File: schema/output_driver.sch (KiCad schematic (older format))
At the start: 9 parts, among them Q3 BC107B, U11 HEF4013, U4 HEF4538

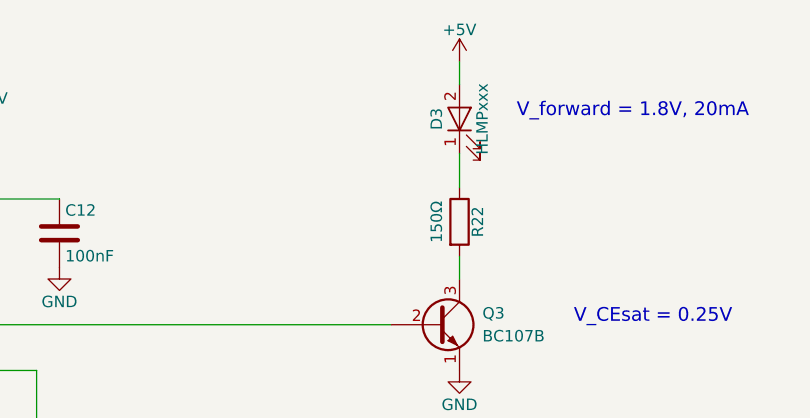
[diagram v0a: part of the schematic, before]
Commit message: Add missing decoupling capacitors
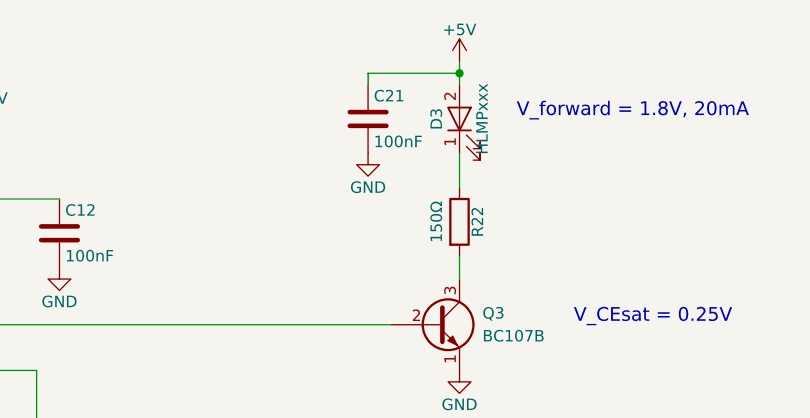
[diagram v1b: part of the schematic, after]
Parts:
- added C21: 100nF, symbol C
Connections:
- wire segments 28 -> 30
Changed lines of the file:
@@
 $EndComp
 $Comp
-L +5V #PWR32
+L +5V #PWR35
 U 1 1 5910A522
 P 8550 2350
-F 0 "#PWR32" H 8550 2200 50  0001 C CNN
+F 0 "#PWR35" H 8550 2200 50  0001 C CNN
 F 1 "+5V" H 8550 2490 50  0000 C CNN
 F 2 "" H 8550 2350 50  0000 C CNN
@@
 $EndComp
 $Comp
-L GND #PWR33
+L GND #PWR36
 U 1 1 5910A53C
 P 8550 3700
-F 0 "#PWR33" H 8550 3450 50  0001 C CNN
+F 0 "#PWR36" H 8550 3450 50  0001 C CNN
 F 1 "GND" H 8550 3550 50  0000 C CNN
 F 2 "" H 8550 3700 50  0000 C CNN
@@
 	2600 2800 2600 2600
 $Comp
-L +5V #PWR22
+L +5V #PWR24
 U 1 1 592FDE80
 P 2600 2700
-F 0 "#PWR22" H 2600 2550 50  0001 C CNN
+F 0 "#PWR24" H 2600 2550 50  0001 C CNN
 F 1 "+5V" H 2600 2840 50  0000 C CNN
 F 2 "" H 2600 2700 50  0000 C CNN
@@
 $EndComp
 $Comp
-L +5V #PWR25
+L +5V #PWR27
 U 1 1 592FE41E
 P 4150 2850
-F 0 "#PWR25" H 4150 2700 50  0001 C CNN
+F 0 "#PWR27" H 4150 2700 50  0001 C CNN
 F 1 "+5V" H 4150 2990 50  0000 C CNN
 F 2 "" H 4150 2850 50  0000 C CNN
@@
 	2800 3800 1750 3800
 $Comp
-L +5V #PWR23
+L +5V #PWR25
 U 1 1 592FE666
 P 2600 3700
-F 0 "#PWR23" H 2600 3550 50  0001 C CNN
+F 0 "#PWR25" H 2600 3550 50  0001 C CNN
 F 1 "+5V" H 2600 3840 50  0000 C CNN
 F 2 "" H 2600 3700 50  0000 C CNN
@@
 $EndComp
 $Comp
-L GND #PWR24
+L GND #PWR26
 U 1 1 592FE7B3
 P 4100 4350
-F 0 "#PWR24" H 4100 4100 50  0001 C CNN
+F 0 "#PWR26" H 4100 4100 50  0001 C CNN
 F 1 "GND" H 4100 4200 50  0000 C CNN
 F 2 "" H 4100 4350 50  0000 C CNN
@@
 Connection ~ 4150 3150
 $Comp
-L GND #PWR26
+L GND #PWR28
 U 1 1 593C9421
 P 4450 3450
-F 0 "#PWR26" H 4450 3200 50  0001 C CNN
+F 0 "#PWR28" H 4450 3200 50  0001 C CNN
 F 1 "GND" H 4450 3300 50  0000 C CNN
 F 2 "" H 4450 3450 50  0000 C CNN
@@
 	5300 3500 5300 4400
 $Comp
-L GND #PWR30
+L GND #PWR32
 U 1 1 593C9562
 P 6500 3900
-F 0 "#PWR30" H 6500 3650 50  0001 C CNN
+F 0 "#PWR32" H 6500 3650 50  0001 C CNN
 F 1 "GND" H 6500 3750 50  0000 C CNN
 F 2 "" H 6500 3900 50  0000 C CNN
@@
 $EndComp
 $Comp
-L GND #PWR31
+L GND #PWR33
 U 1 1 593C9588
 P 6800 3250
-F 0 "#PWR31" H 6800 3000 50  0001 C CNN
+F 0 "#PWR33" H 6800 3000 50  0001 C CNN
 F 1 "GND" H 6800 3100 50  0000 C CNN
 F 2 "" H 6800 3250 50  0000 C CNN
@@
 Connection ~ 6500 2950
 $Comp
-L +5V #PWR29
+L +5V #PWR31
 U 1 1 593C9631
 P 6500 2650
-F 0 "#PWR29" H 6500 2500 50  0001 C CNN
+F 0 "#PWR31" H 6500 2500 50  0001 C CNN
 F 1 "+5V" H 6500 2790 50  0000 C CNN
 F 2 "" H 6500 2650 50  0000 C CNN
@@
 Connection ~ 2750 3700
 $Comp
-L GND #PWR28
+L GND #PWR30
 U 1 1 593CBF84
 P 5950 4200
-F 0 "#PWR28" H 5950 3950 50  0001 C CNN
+F 0 "#PWR30" H 5950 3950 50  0001 C CNN
 F 1 "GND" H 5950 4050 50  0000 C CNN
 F 2 "" H 5950 4200 50  0000 C CNN
@@
 $EndComp
 $Comp
-L GND #PWR27
+L GND #PWR29
 U 1 1 593CC00A
 P 5750 2950
-F 0 "#PWR27" H 5750 2700 50  0001 C CNN
+F 0 "#PWR29" H 5750 2700 50  0001 C CNN
 F 1 "GND" H 5750 2800 50  0000 C CNN
 F 2 "" H 5750 2950 50  0000 C CNN
@@
 Wire Wire Line
 	5950 2950 5950 3000
+$Comp
+L C C21
+U 1 1 593EC611
+P 8150 2600
+F 0 "C21" H 8175 2700 50  0000 L CNN
+F 1 "100nF" H 8175 2500 50  0000 L CNN
+F 2 "" H 8188 2450 50  0000 C CNN
+F 3 "" H 8150 2600 50  0000 C CNN
+	1    8150 2600
+	1    0    0    -1
+$EndComp
+Wire Wire Line
+	8150 2450 8150 2400
+Wire Wire Line
+	8150 2400 8550 2400
+Connection ~ 8550 2400
+$Comp
+L GND #PWR34
+U 1 1 593EC685
+P 8150 2750
+F 0 "#PWR34" H 8150 2500 50  0001 C CNN
+F 1 "GND" H 8150 2600 50  0000 C CNN
+F 2 "" H 8150 2750 50  0000 C CNN
+F 3 "" H 8150 2750 50  0000 C CNN
+	1    8150 2750
+	1    0    0    -1
+$EndComp
 $EndSCHEMATC
